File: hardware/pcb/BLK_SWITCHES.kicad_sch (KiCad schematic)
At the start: 36 parts, among them J12 IDC-20_SWITCH_BUS, J13 IDC-12_SWITCH_ZONE_BUS, U11 MCP23017_ML

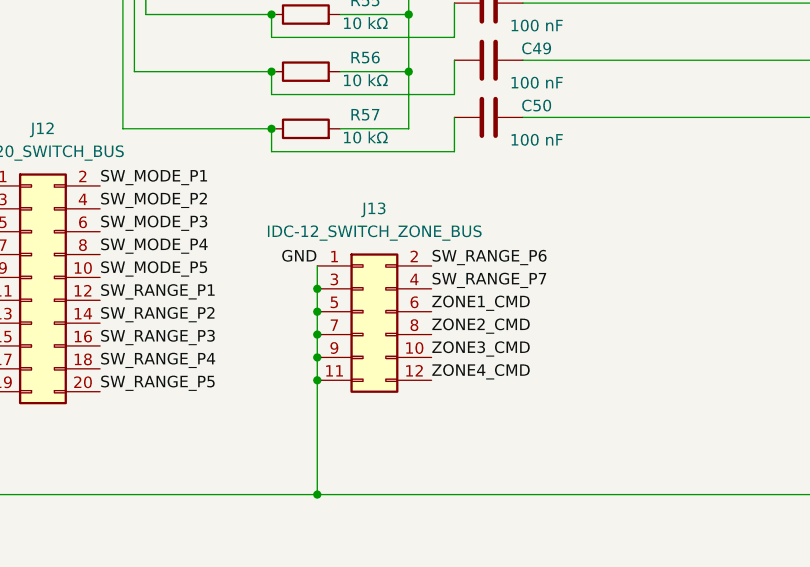
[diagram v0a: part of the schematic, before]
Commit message: Update hardware schematics and documentation; added source of truth for hardware, removed unused symbols, and modified connector specifications.
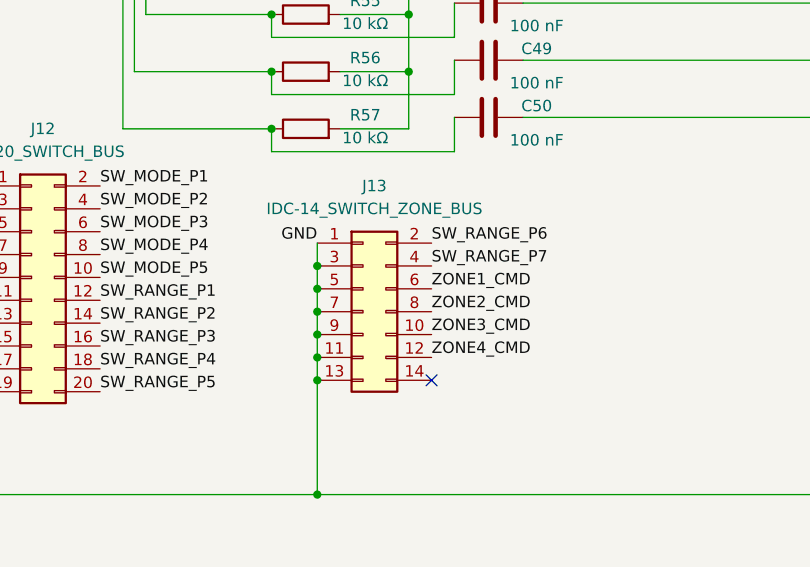
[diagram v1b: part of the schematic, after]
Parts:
- J13: value IDC-12_SWITCH_ZONE_BUS -> IDC-14_SWITCH_ZONE_BUS; footprint Connector_IDC:IDC-Header_2x06_P2.54mm_Vertical -> Connector_IDC:IDC-Header_2x07_P2.54mm_Vertical; symbol Connector_Generic:Conn_02x06_Odd_Even -> Connector_Generic:Conn_02x07_Odd_Even
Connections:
- net GND: now also J13.13 (Pin_13)
- no-connect marks 3 -> 4
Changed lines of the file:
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@@
 	)
 	(junction
+		(at 142.24 156.21)
+		(diameter 0)
+		(color 0 0 0 0)
+	)
+	(junction
 		(at 105.41 165.1)
 		(diameter 0)
@@
 	)
 	(no_connect
+		(at 154.94 168.91)
+	)
+	(no_connect
 		(at 77.47 74.93)
 	)
@@
 	(wire
 		(pts
+			(xy 142.24 153.67) (xy 142.24 156.21)
+		)
+		(stroke
+			(width 0)
+			(type default)
+		)
+	)
+	(wire
+		(pts
 			(xy 157.48 92.71) (xy 137.16 92.71)
 		)
@@
 		)
 	)
-	(label "ZONE1_CMD"
-		(at 154.94 161.29 0)
+	(label "ZONE4_CMD"
+		(at 154.94 166.37 0)
 		(effects
 			(font
@@
 		)
 	)
-	(label "SW_RANGE_P7"
-		(at 154.94 158.75 0)
+	(label "SW_RANGE_P2"
+		(at 118.11 162.56 0)
 		(effects
 			(font
@@
 		)
 	)
-	(label "SW_RANGE_P2"
-		(at 118.11 162.56 0)
+	(label "SW_MODE_P2"
+		(at 113.03 95.25 0)
 		(effects
 			(font
@@
 		)
 	)
-	(label "ZONE3_CMD"
-		(at 154.94 166.37 0)
+	(label "SW_RANGE_P5"
+		(at 118.11 170.18 0)
 		(effects
 			(font
@@
 		)
 	)
-	(label "SW_MODE_P2"
-		(at 113.03 95.25 0)
+	(label "SW_RANGE_P6"
+		(at 154.94 153.67 0)
 		(effects
 			(font
@@
 		)
 	)
-	(label "SW_RANGE_P5"
-		(at 118.11 170.18 0)
+	(label "GND"
+		(at 105.41 147.32 180)
 		(effects
 			(font
 				(size 1.27 1.27)
 			)
-			(justify left bottom)
+			(justify right bottom)
 		)
 	)
-	(label "GND"
-		(at 105.41 147.32 180)
+	(label "ZONE2_CMD"
+		(at 154.94 161.29 0)
 		(effects
 			(font
 				(size 1.27 1.27)
 			)
-			(justify right bottom)
+			(justify left bottom)
 		)
 	)
-	(label "SW_RANGE_P4"
-		(at 113.03 57.15 0)
+	(label "SW_RANGE_P7"
+		(at 154.94 156.21 0)
 		(effects
 			(font
@@
 		)
 	)
-	(label "SW_MODE_P5"
-		(at 118.11 157.48 0)
+	(label "SW_RANGE_P4"
+		(at 113.03 57.15 0)
 		(effects
 			(font
@@
 		)
 	)
-	(label "SW_MODE_P4"
-		(at 113.03 90.17 0)
+	(label "SW_MODE_P5"
+		(at 118.11 157.48 0)
 		(effects
 			(font
@@
 		)
 	)
-	(label "SW_RANGE_P6"
-		(at 154.94 156.21 0)
+	(label "SW_MODE_P4"
+		(at 113.03 90.17 0)
 		(effects
 			(font
@@
 		)
 	)
-	(label "GND"
-		(at 142.24 156.21 180)
-		(effects
-			(font
-				(size 1.27 1.27)
-			)
-			(justify right bottom)
-		)
-	)
 	(label "SW_RANGE_P1"
 		(at 113.03 85.09 0)
@@
 	)
 	(label "ZONE2_CMD"
-		(at 154.94 163.83 0)
+		(at 113.03 69.85 0)
 		(effects
 			(font
@@
 		)
 	)
-	(label "ZONE2_CMD"
-		(at 113.03 69.85 0)
+	(label "SW_RANGE_P2"
+		(at 113.03 82.55 0)
 		(effects
 			(font
@@
 		)
 	)
-	(label "SW_RANGE_P2"
-		(at 113.03 82.55 0)
+	(label "SW_RANGE_P1"
+		(at 118.11 160.02 0)
 		(effects
 			(font
@@
 		)
 	)
-	(label "SW_RANGE_P1"
-		(at 118.11 160.02 0)
+	(label "GND"
+		(at 142.24 153.67 180)
 		(effects
 			(font
 				(size 1.27 1.27)
 			)
-			(justify left bottom)
+			(justify right bottom)
 		)
 	)
@@
 		)
 	)
+	(label "ZONE3_CMD"
+		(at 154.94 163.83 0)
+		(effects
+			(font
+				(size 1.27 1.27)
+			)
+			(justify left bottom)
+		)
+	)
 	(label "SW_RANGE_P3"
 		(at 118.11 165.1 0)
@@
 		)
 	)
-	(label "ZONE4_CMD"
-		(at 154.94 168.91 0)
+	(label "ZONE1_CMD"
+		(at 113.03 67.31 0)
 		(effects
 			(font
@@
 	)
 	(label "ZONE1_CMD"
-		(at 113.03 67.31 0)
+		(at 154.94 158.75 0)
 		(effects
 			(font
@@
 	)
 	(symbol
-		(lib_id "Connector_Generic:Conn_02x06_Odd_Even")
+		(lib_id "Connector_Generic:Conn_02x07_Odd_Even")
 		(at 147.32 161.29 0)
 		(unit 1)
@@
 		(fields_autoplaced yes)
 		(property "Reference" "J13"
-			(at 148.59 149.86 0)
+			(at 148.59 147.32 0)
 			(effects
 				(font
@@
 			)
 		)
-		(property "Value" "IDC-12_SWITCH_ZONE_BUS"
-			(at 148.59 152.4 0)
+		(property "Value" "IDC-14_SWITCH_ZONE_BUS"
+			(at 148.59 149.86 0)
 			(effects
 				(font
@@
 			)
 		)
-		(property "Footprint" "Connector_IDC:IDC-Header_2x06_P2.54mm_Vertical"
+		(property "Footprint" "Connector_IDC:IDC-Header_2x07_P2.54mm_Vertical"
 			(at 147.32 161.29 0)
 			(effects
@@
 			)
 		)
-		(property "Description" "Generic connector, double row, 02x06, odd/even pin numbering scheme (row 1 odd numbers, row 2 even numbers), script generated (kicad-library-utils/schlib/autogen/connector/)"
+		(property "Description" "Generic connector, double row, 02x07, odd/even pin numbering scheme (row 1 odd numbers, row 2 even numbers), script generated (kicad-library-utils/schlib/autogen/connector/)"
 			(at 147.32 161.29 0)
 			(effects
@@
 		(pin "8"
 		)
+		(pin "13"
+		)
+		(pin "14"
+		)
 		(instances
